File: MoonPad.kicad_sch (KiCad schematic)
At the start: 59 parts, among them IC1 W25Q16JVUXIQ, J1 OLED, J3 USB-C 2.0 Receptacle, SW1 Reset, U3 RP2040, U4 SLSS49E-3, U5 SLSS49E-3, U6 AP2112K-3.3, Y1 JGHC S3212000181080

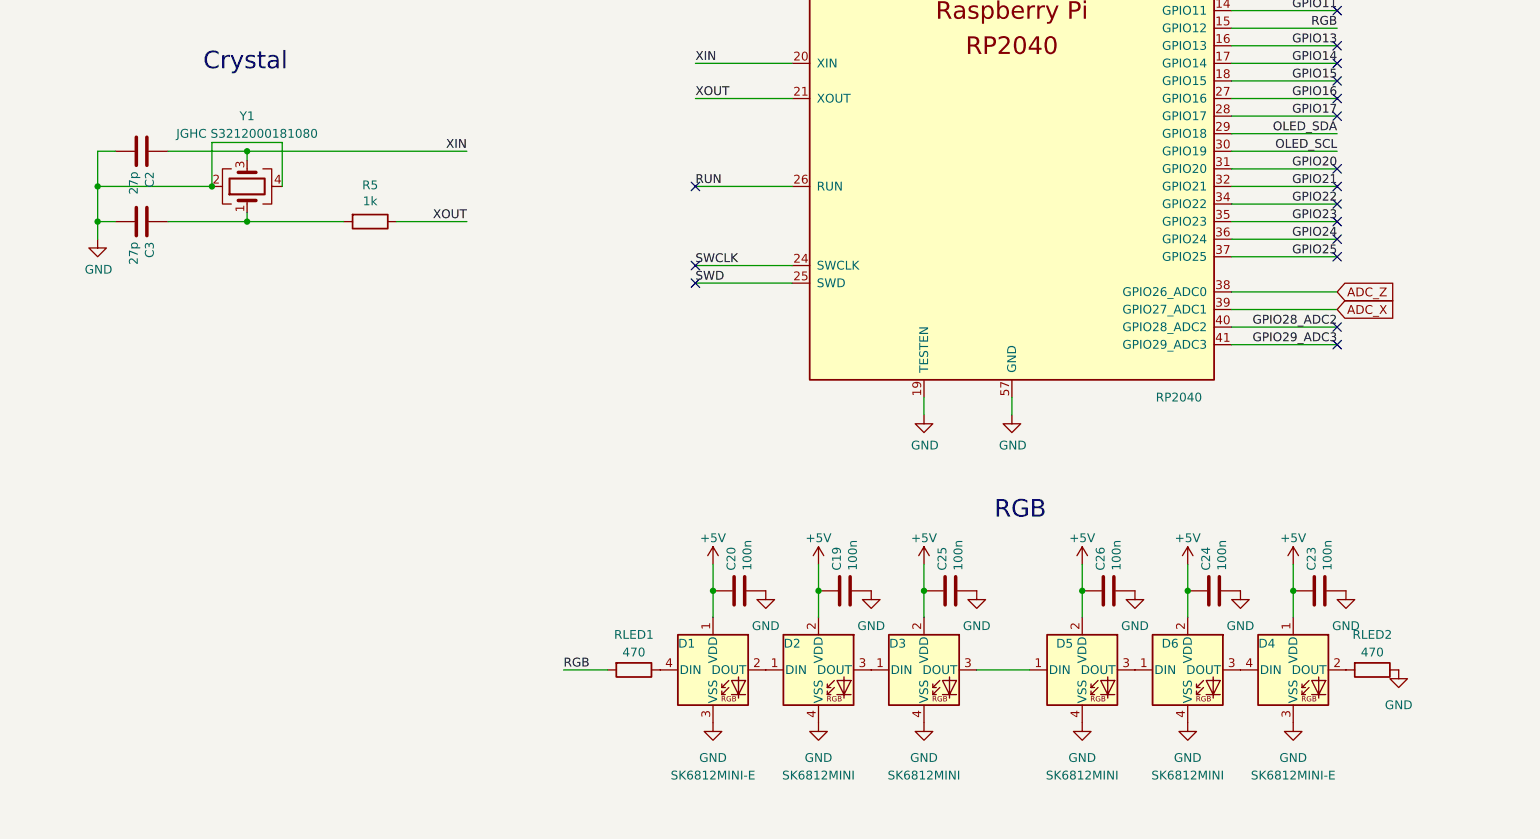
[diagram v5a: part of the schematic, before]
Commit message: Cost optimisation + case files
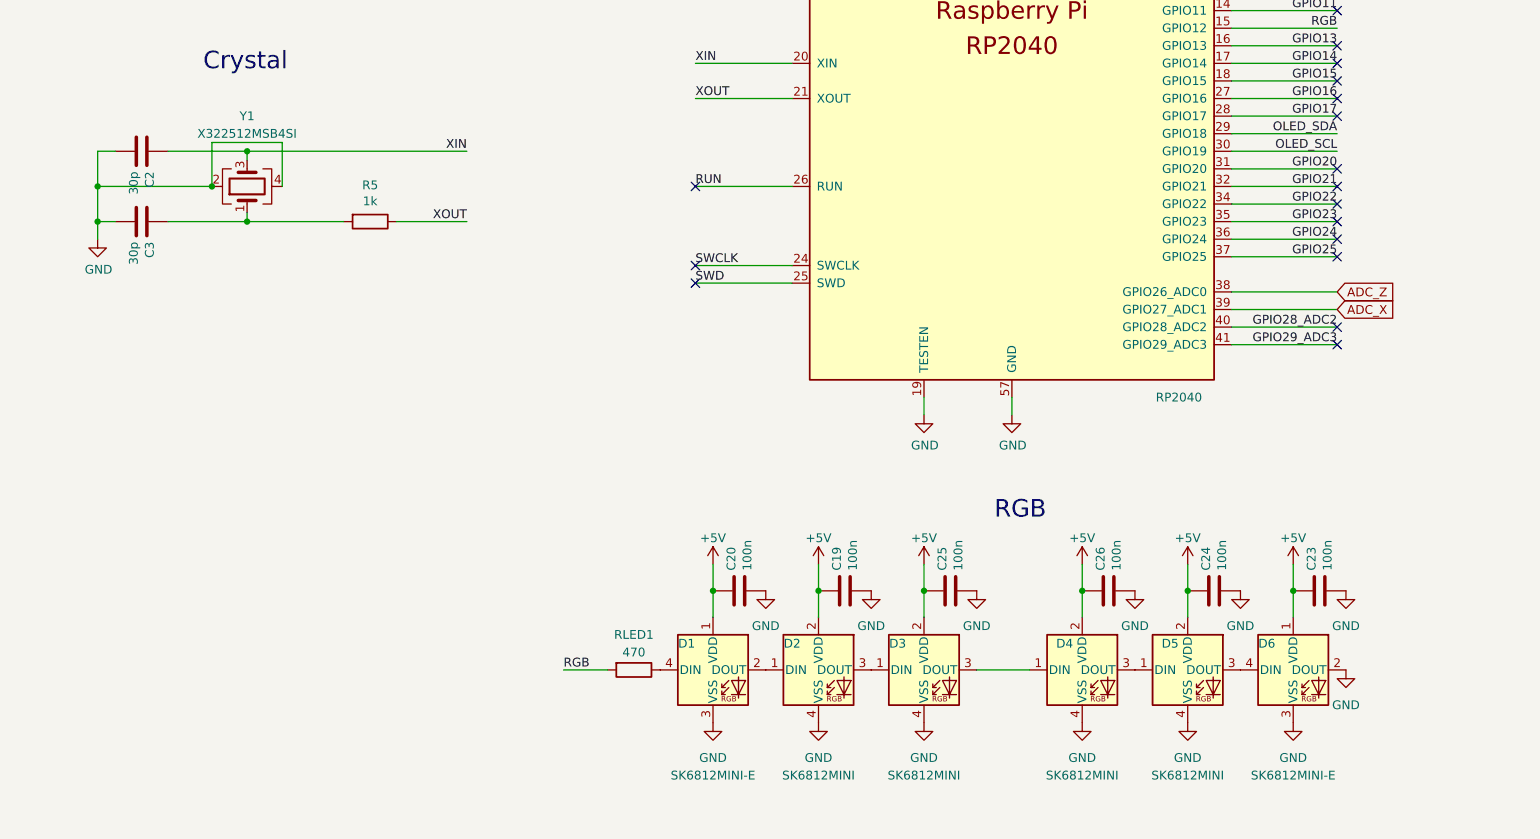
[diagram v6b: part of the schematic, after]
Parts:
- removed RLED2: 470, Resistor_SMD:R_0402_1005Metric, symbol Device:R
- C17, C18: LCSC C5139511 -> C1525
- C2, C3: value 27p -> 30p; LCSC C86287 -> C1570
- D1: LCSC C5149201 -> C5378731; LCSC Part C5149201 -> (none)
- D2, D3: LCSC C5183448 -> C2886570; LCSC Part C5183448 -> (none)
- D4: renamed from D5; LCSC C5183448 -> C2886570; LCSC Part C5183448 -> (none)
- D5: renamed from D6; LCSC C5183448 -> C2886570; LCSC Part C5183448 -> (none)
- D6: renamed from D4; LCSC C5149201 -> C5378731; LCSC Part C5149201 -> (none)
- IC1: LCSC Part C2843335 -> (none)
- J3: LCSC Part C165948 -> (none)
- R1, R5: LCSC C25543 -> C11702; LCSC Part C25543 -> (none)
- R3, R4: LCSC Part C25100 -> (none)
- RLED1: LCSC C2828857 -> C25117
- SW1: LCSC C115351 -> C318884
- U3: LCSC Part C2040 -> (none)
- U4, U5: LCSC Part C2904393 -> (none)
- Y1: value JGHC S3212000181080 -> X322512MSB4SI; LCSC C390764 -> C9002; LCSC Part C390764 -> (none)
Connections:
- net GND: now also D6.2 (DOUT)
